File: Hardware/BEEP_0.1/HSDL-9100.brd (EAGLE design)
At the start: 21.3 x 23.6 mm, 9 parts, among them IC1 HSDL-9100

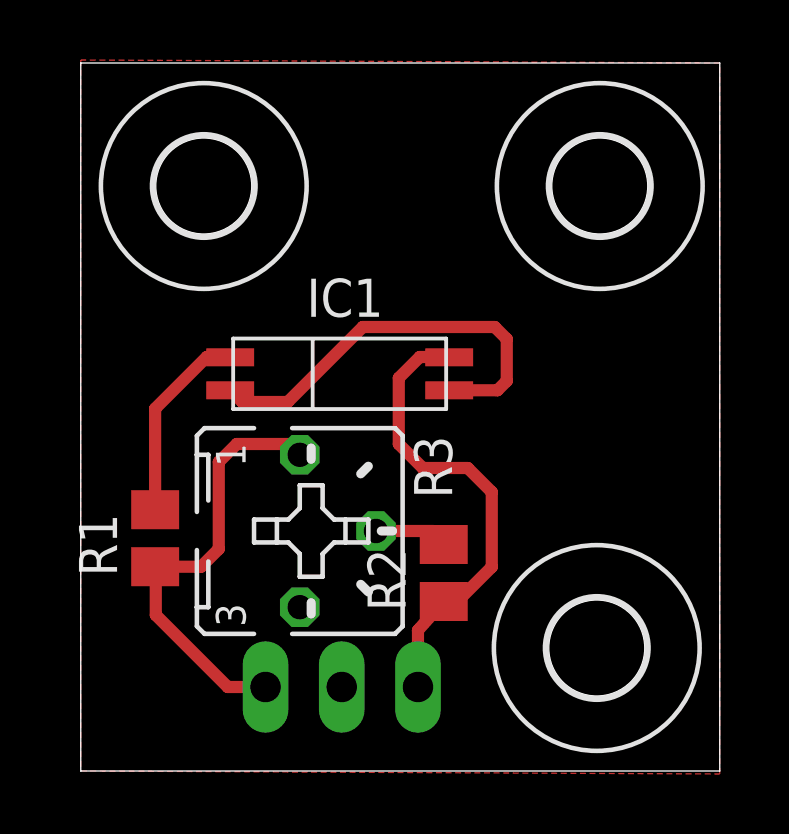
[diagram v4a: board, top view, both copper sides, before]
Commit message: enhance pads and board for HSDL-9100
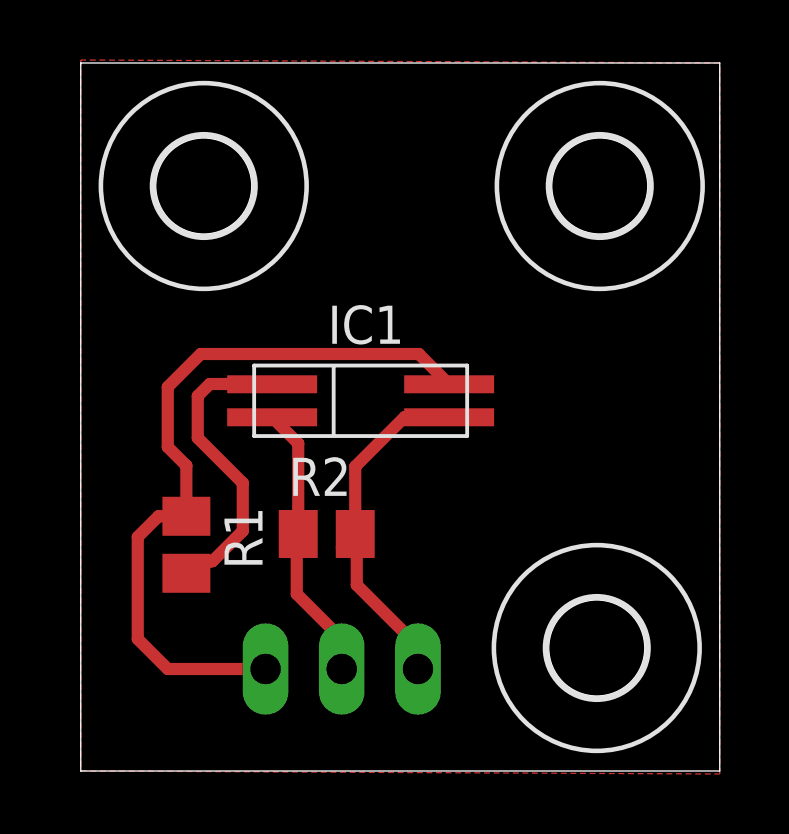
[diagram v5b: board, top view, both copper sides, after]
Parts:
- removed R3: (no value), pot:B25P
- moved R2 4.11 mm to (8.20, 7.90), turned to 0 degrees
- moved IC1 1.14 mm to (9.33, 12.3)
- moved R1 1.06 mm to (3.52, 7.54), turned to 270 degrees
- moved JP1 0.60 mm to (8.70, 3.40)
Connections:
- removed net N$5: R2.2, R3.S
- net ADATA: now also IC1.DET_A, R2.2; no longer IC1.DET_K, R2.1
- net GND: now also R2.1; no longer IC1.DET_A
- net VCC: now also IC1.DET_K; no longer R3.A
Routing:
- net VCC: track 14.9 -> 24.8 mm
- net GND: track 14.0 -> 9.39 mm
- net ADATA: track 15.8 -> 12.1 mm
- net N$3: track 6.58 -> 10.2 mm
- net N$5: track 2.48 -> 0.00 mm
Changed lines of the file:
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@@
 <vertex x="21.3" y="7.5"/>
 </polygon>
-<wire x1="4.3" y1="14.4" x2="6" y2="14.4" width="0.4064" layer="41"/>
-<wire x1="6" y1="14.4" x2="6" y2="13.4" width="0.4064" layer="41"/>
-<wire x1="6" y1="13.4" x2="6.4" y2="13.4" width="0.4064" layer="41"/>
-<wire x1="6.4" y1="13.4" x2="6.4" y2="14.4" width="0.4064" layer="41"/>
-<wire x1="13.3" y1="14.3" x2="10.8" y2="14.3" width="0.4064" layer="41"/>
-<wire x1="10.8" y1="14.3" x2="10.8" y2="13.7" width="0.4064" layer="41"/>
-<wire x1="13.3" y1="14.3" x2="13.3" y2="13.4" width="0.4064" layer="41"/>
+<wire x1="8.1" y1="11.1" x2="9.2" y2="11.1" width="0.4064" layer="41"/>
+<wire x1="9.2" y1="11.1" x2="9.8" y2="11.7" width="0.4064" layer="41"/>
+<wire x1="8.1" y1="11.1" x2="8.1" y2="13.4" width="0.4064" layer="41"/>
 </plain>
 <attributes>
@@
 </autorouter>
 <elements>
-<element name="IC1" library="BEEP" package="HSDL-9100" value="HSDL-9100" x="8.63" y="13.24" smashed="yes">
-<attribute name="NAME" x="7.53" y="15.14" size="1.27" layer="25"/>
-<attribute name="VALUE" x="3.83" y="10.14" size="1.27" layer="27"/>
+<element name="IC1" library="BEEP" package="HSDL-9100" value="HSDL-9100" x="9.33" y="12.34" smashed="yes">
+<attribute name="NAME" x="8.23" y="14.24" size="1.27" layer="25"/>
+<attribute name="VALUE" x="4.53" y="9.24" size="1.27" layer="27"/>
 </element>
-<element name="R1" library="rcl" package="M0805" value="" x="2.48" y="7.76" rot="R90"/>
-<element name="JP1" library="pinhead" package="1X03" value="" x="8.7" y="2.8" smashed="yes" rot="MR180">
-<attribute name="VALUE" x="4.89" y="5.975" size="1.27" layer="28" rot="MR180"/>
+<element name="R1" library="rcl" package="M0805" value="" x="3.52" y="7.54" rot="R270"/>
+<element name="JP1" library="pinhead" package="1X03" value="" x="8.7" y="3.4" smashed="yes" rot="MR180">
+<attribute name="VALUE" x="4.89" y="6.575" size="1.27" layer="28" rot="MR180"/>
 </element>
 <element name="U$2" library="holes" package="3,2" value="" x="17.2" y="4.1"/>
@@
 <element name="U$4" library="holes" package="3,2" value="" x="17.3" y="19.5"/>
 <element name="U$1" library="Branding" package="COPPER3" value="LOGO-COPPER3" x="15.1" y="12.6"/>
-<element name="R2" library="rcl" package="M0805" value="" x="12.1" y="6.6" rot="R90"/>
-<element name="R3" library="pot" package="B25P" value="" x="7.3" y="8" rot="R270"/>
+<element name="R2" library="rcl" package="M0805" value="" x="8.2" y="7.9"/>
 </elements>
 <signals>
@@
 <contactref element="IC1" pad="LED_A"/>
 <contactref element="R1" pad="2"/>
-<wire x1="2.48" y1="8.71" x2="2.48" y2="12.08" width="0.4064" layer="1"/>
-<wire x1="2.48" y1="12.08" x2="4.2" y2="13.8" width="0.4064" layer="1"/>
-<wire x1="4.2" y1="13.8" x2="4.94" y2="13.8" width="0.4064" layer="1"/>
-<wire x1="4.94" y1="13.8" x2="4.98" y2="13.79" width="0.4064" layer="1"/>
+<wire x1="3.52" y1="6.59" x2="4.29" y2="6.99" width="0.4064" layer="1"/>
+<wire x1="4.3" y1="12.9" x2="6.37" y2="12.9" width="0.4064" layer="1"/>
+<wire x1="6.37" y1="12.9" x2="6.38" y2="12.89" width="0.4064" layer="1"/>
+<wire x1="4.29" y1="6.99" x2="4.39" y2="6.99" width="0.4064" layer="1"/>
+<wire x1="4.39" y1="6.99" x2="5.4" y2="8" width="0.4064" layer="1"/>
+<wire x1="5.4" y1="8" x2="5.4" y2="9.6" width="0.4064" layer="1"/>
+<wire x1="5.4" y1="9.6" x2="3.9" y2="11.1" width="0.4064" layer="1"/>
+<wire x1="3.9" y1="11.1" x2="3.9" y2="12.5" width="0.4064" layer="1"/>
+<wire x1="3.9" y1="12.5" x2="4.3" y2="12.9" width="0.4064" layer="1"/>
 </signal>
 <signal name="GND">
@@
 </polygon>
 <contactref element="IC1" pad="LED_K"/>
+<contactref element="R2" pad="1"/>
+<wire x1="7.25" y1="7.9" x2="7.25" y2="10.92" width="0.4064" layer="1"/>
+<wire x1="7.25" y1="10.92" x2="6.38" y2="11.79" width="0.4064" layer="1"/>
+<contactref element="JP1" pad="2"/>
+<wire x1="8.7" y1="3.4" x2="8.7" y2="4.4" width="0.4064" layer="1"/>
+<wire x1="8.7" y1="4.4" x2="7.2" y2="5.9" width="0.4064" layer="1"/>
+<wire x1="7.2" y1="5.9" x2="7.2" y2="7.85" width="0.4064" layer="1"/>
+<wire x1="7.2" y1="7.85" x2="7.25" y2="7.9" width="0.4064" layer="1"/>
+</signal>
+<signal name="ADATA">
 <contactref element="IC1" pad="DET_A"/>
-<wire x1="12.28" y1="12.69" x2="13.89" y2="12.69" width="0.4064" layer="1"/>
-<wire x1="13.89" y1="12.69" x2="14.2" y2="13" width="0.4064" layer="1"/>
-<wire x1="14.2" y1="13" x2="14.2" y2="14.4" width="0.4064" layer="1"/>
-<wire x1="14.2" y1="14.4" x2="13.8" y2="14.8" width="0.4064" layer="1"/>
-<wire x1="13.8" y1="14.8" x2="9.4" y2="14.8" width="0.4064" layer="1"/>
-<wire x1="9.4" y1="14.8" x2="6.9" y2="12.3" width="0.4064" layer="1"/>
-<wire x1="6.9" y1="12.3" x2="5.39" y2="12.3" width="0.4064" layer="1"/>
-<wire x1="5.39" y1="12.3" x2="4.98" y2="12.69" width="0.4064" layer="1"/>
-<contactref element="JP1" pad="2"/>
-</signal>
-<signal name="ADATA">
-<contactref element="IC1" pad="DET_K"/>
-<contactref element="R2" pad="1"/>
-<wire x1="12.05" y1="5.5" x2="12.1" y2="5.65" width="0.4064" layer="1"/>
-<wire x1="12.1" y1="5.65" x2="12.55" y2="5.65" width="0.4064" layer="1"/>
-<wire x1="12.55" y1="5.65" x2="13.7" y2="6.8" width="0.4064" layer="1"/>
-<wire x1="13.7" y1="6.8" x2="13.7" y2="9.3" width="0.4064" layer="1"/>
-<wire x1="13.7" y1="9.3" x2="12.9" y2="10.1" width="0.4064" layer="1"/>
-<wire x1="12.9" y1="10.1" x2="11.4" y2="10.1" width="0.4064" layer="1"/>
-<wire x1="11.4" y1="10.1" x2="10.6" y2="10.9" width="0.4064" layer="1"/>
-<wire x1="10.6" y1="10.9" x2="10.6" y2="13.1" width="0.4064" layer="1"/>
-<wire x1="10.6" y1="13.1" x2="11.3" y2="13.8" width="0.4064" layer="1"/>
-<wire x1="11.3" y1="13.8" x2="12.17" y2="13.8" width="0.4064" layer="1"/>
-<wire x1="12.17" y1="13.8" x2="12.28" y2="13.79" width="0.4064" layer="1"/>
+<contactref element="R2" pad="2"/>
+<wire x1="8.7" y1="7.45" x2="9.15" y2="7.9" width="0.4064" layer="1"/>
+<wire x1="9.15" y1="7.9" x2="9.15" y2="10.15" width="0.4064" layer="1"/>
+<wire x1="9.15" y1="10.15" x2="10.8" y2="11.8" width="0.4064" layer="1"/>
+<wire x1="10.8" y1="11.8" x2="12.27" y2="11.8" width="0.4064" layer="1"/>
+<wire x1="12.27" y1="11.8" x2="12.28" y2="11.79" width="0.4064" layer="1"/>
 <contactref element="JP1" pad="3"/>
-<wire x1="11.24" y1="2.8" x2="11.24" y2="4.69" width="0.4064" layer="1"/>
-<wire x1="11.24" y1="4.69" x2="12.1" y2="5.65" width="0.4064" layer="1"/>
-</signal>
-<signal name="N$5">
-<contactref element="R2" pad="2"/>
-<contactref element="R3" pad="S"/>
-<wire x1="9.84" y1="8" x2="11.75" y2="8" width="0.4064" layer="1"/>
-<wire x1="11.75" y1="8" x2="12.1" y2="7.55" width="0.4064" layer="1"/>
+<wire x1="11.24" y1="3.4" x2="11.24" y2="4.16" width="0.4064" layer="1"/>
+<wire x1="11.24" y1="4.16" x2="9.2" y2="6.2" width="0.4064" layer="1"/>
+<wire x1="9.2" y1="6.2" x2="9.2" y2="7.85" width="0.4064" layer="1"/>
+<wire x1="9.2" y1="7.85" x2="9.15" y2="7.9" width="0.4064" layer="1"/>
 </signal>
 <signal name="VCC">
-<contactref element="R3" pad="A"/>
 <contactref element="R1" pad="1"/>
 <contactref element="JP1" pad="1"/>
-<wire x1="6.16" y1="2.8" x2="4.9" y2="2.8" width="0.4064" layer="1"/>
-<wire x1="4.9" y1="2.8" x2="2.5" y2="5.2" width="0.4064" layer="1"/>
-<wire x1="2.5" y1="5.2" x2="2.5" y2="6.49" width="0.4064" layer="1"/>
-<wire x1="2.5" y1="6.49" x2="2.48" y2="6.81" width="0.4064" layer="1"/>
-<wire x1="2.48" y1="6.81" x2="4.01" y2="6.81" width="0.4064" layer="1"/>
-<wire x1="4.01" y1="6.81" x2="4.6" y2="7.4" width="0.4064" layer="1"/>
-<wire x1="4.6" y1="7.4" x2="4.6" y2="10.3" width="0.4064" layer="1"/>
-<wire x1="4.6" y1="10.3" x2="5.2" y2="10.9" width="0.4064" layer="1"/>
-<wire x1="5.2" y1="10.9" x2="7.34" y2="10.9" width="0.4064" layer="1"/>
-<wire x1="7.34" y1="10.9" x2="7.3" y2="10.54" width="0.4064" layer="1"/>
+<contactref element="IC1" pad="DET_K"/>
+<wire x1="11.27" y1="13.9" x2="12.28" y2="12.89" width="0.4064" layer="1"/>
+<wire x1="3.52" y1="8.49" x2="2.59" y2="8.49" width="0.4064" layer="1"/>
+<wire x1="2.59" y1="8.49" x2="1.9" y2="7.8" width="0.4064" layer="1"/>
+<wire x1="6.16" y1="3.4" x2="2.9" y2="3.4" width="0.4064" layer="1"/>
+<wire x1="2.9" y1="3.4" x2="1.9" y2="4.4" width="0.4064" layer="1"/>
+<wire x1="1.9" y1="4.4" x2="1.9" y2="7.8" width="0.4064" layer="1"/>
+<wire x1="4" y1="13.9" x2="11.27" y2="13.9" width="0.4064" layer="1"/>
+<wire x1="3.52" y1="8.49" x2="3.52" y2="10.18" width="0.4064" layer="1"/>
+<wire x1="3.52" y1="10.18" x2="2.9" y2="10.8" width="0.4064" layer="1"/>
+<wire x1="2.9" y1="10.8" x2="2.9" y2="12.8" width="0.4064" layer="1"/>
+<wire x1="2.9" y1="12.8" x2="4" y2="13.9" width="0.4064" layer="1"/>
 </signal>
 </signals>
